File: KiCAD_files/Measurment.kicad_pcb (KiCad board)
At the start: 2 copper layers, 90 x 63 mm, 69 parts, among them J1 Measurment_stage_outline_outp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, J2 Measurment_stage_outline_sign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, J3 Conn_01x02, U1 NMA1505SC, U2 AMC1100, U3 AMC1100, U4 AMC1311, U5 R-78C5.0-1.0, U6 AMS1117-3.3, U7 NMA1505SC

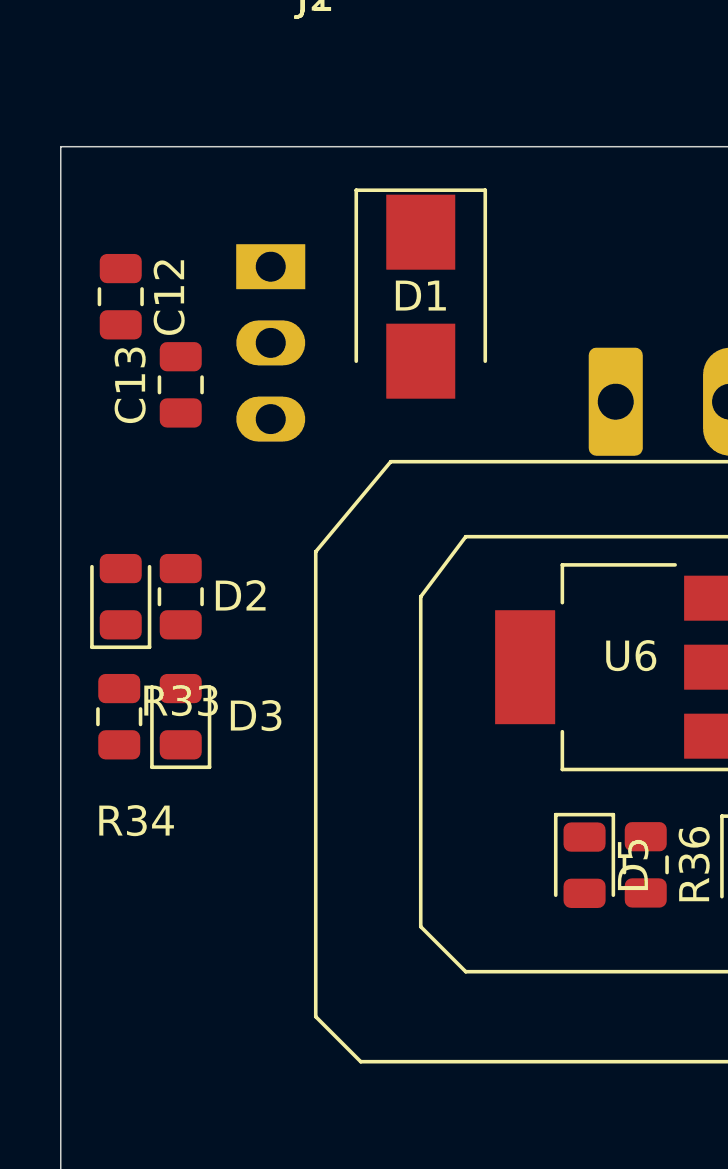
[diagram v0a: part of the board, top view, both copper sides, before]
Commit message: Added alpha version of Nucleo Shield stage - Routed power board
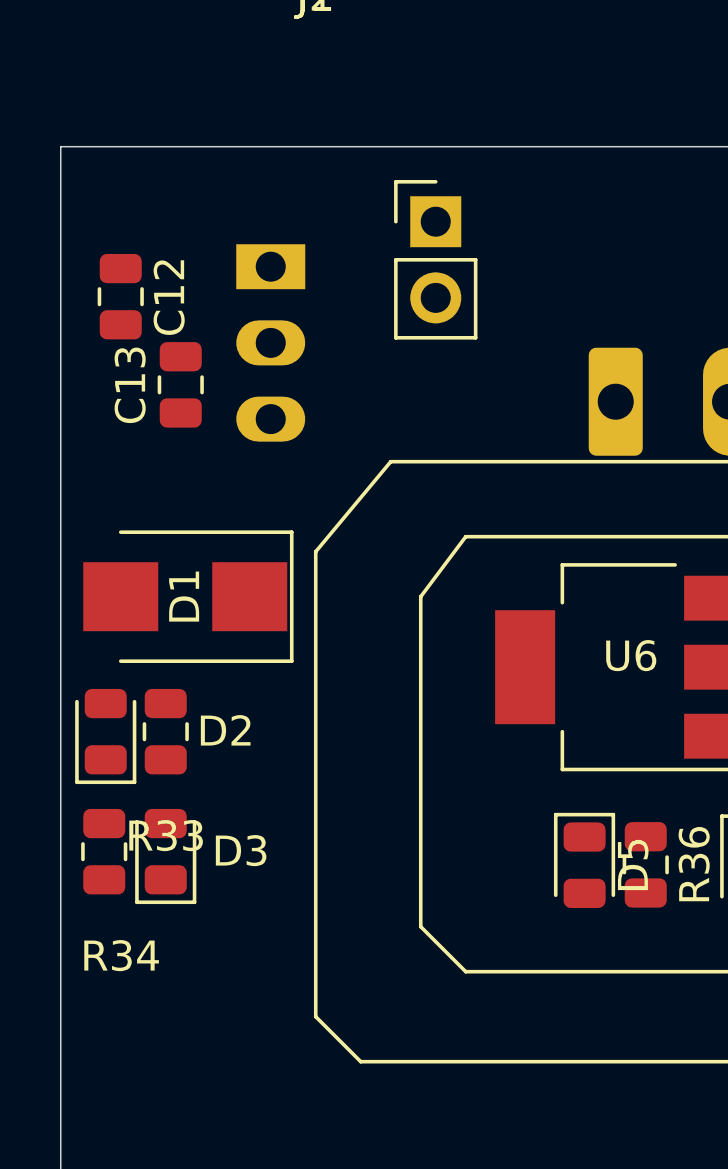
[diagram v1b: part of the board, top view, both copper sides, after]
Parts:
- J1: value Measurment_stage_outline_outputs -> Board outline
- moved D1 12.7 mm to (35.6, 56.5), turned to 180 degrees
- moved D2 4.53 mm to (33.0, 61.0)
- moved D3 4.53 mm to (35.0, 65.0)
- moved R33 4.53 mm to (35.0, 61.0)
- moved R34 4.53 mm to (33.0, 65.0)

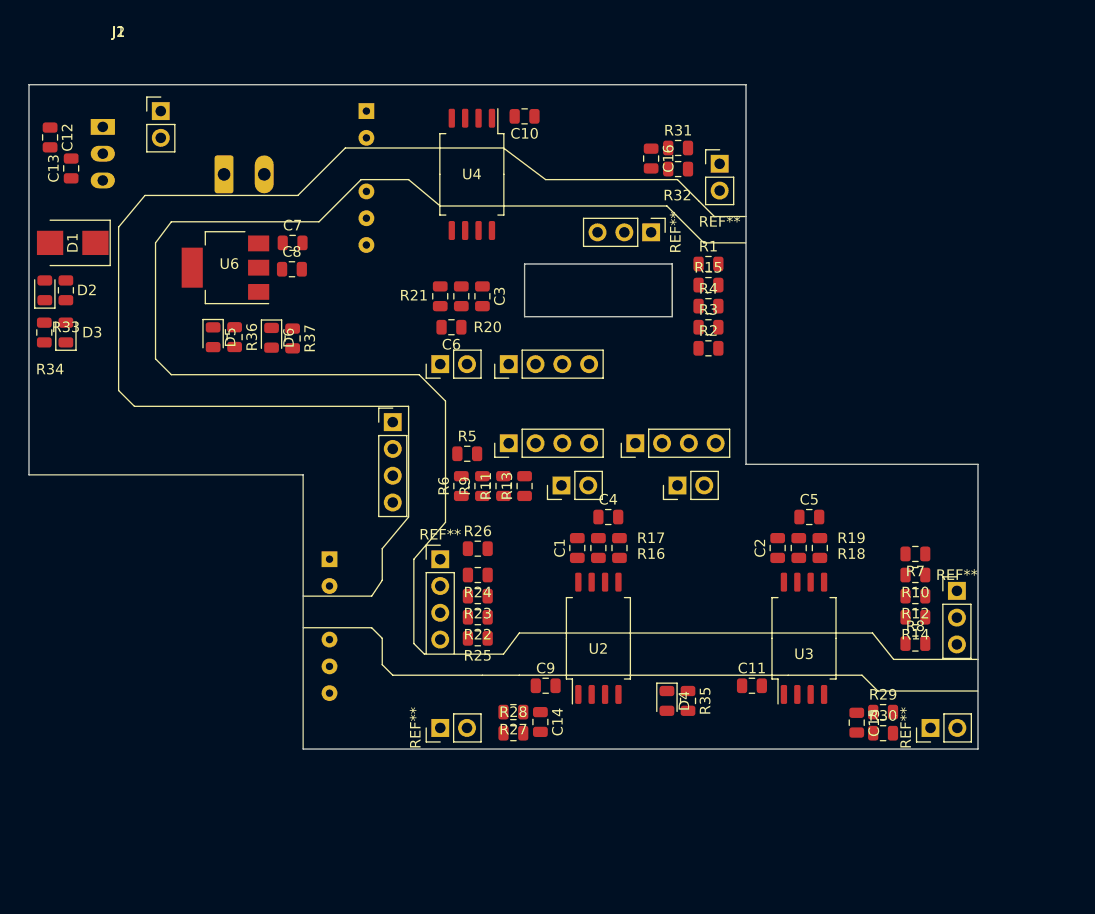
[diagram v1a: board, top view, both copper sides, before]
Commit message: Preliminary routing done - inter layers connectors issues to be solved
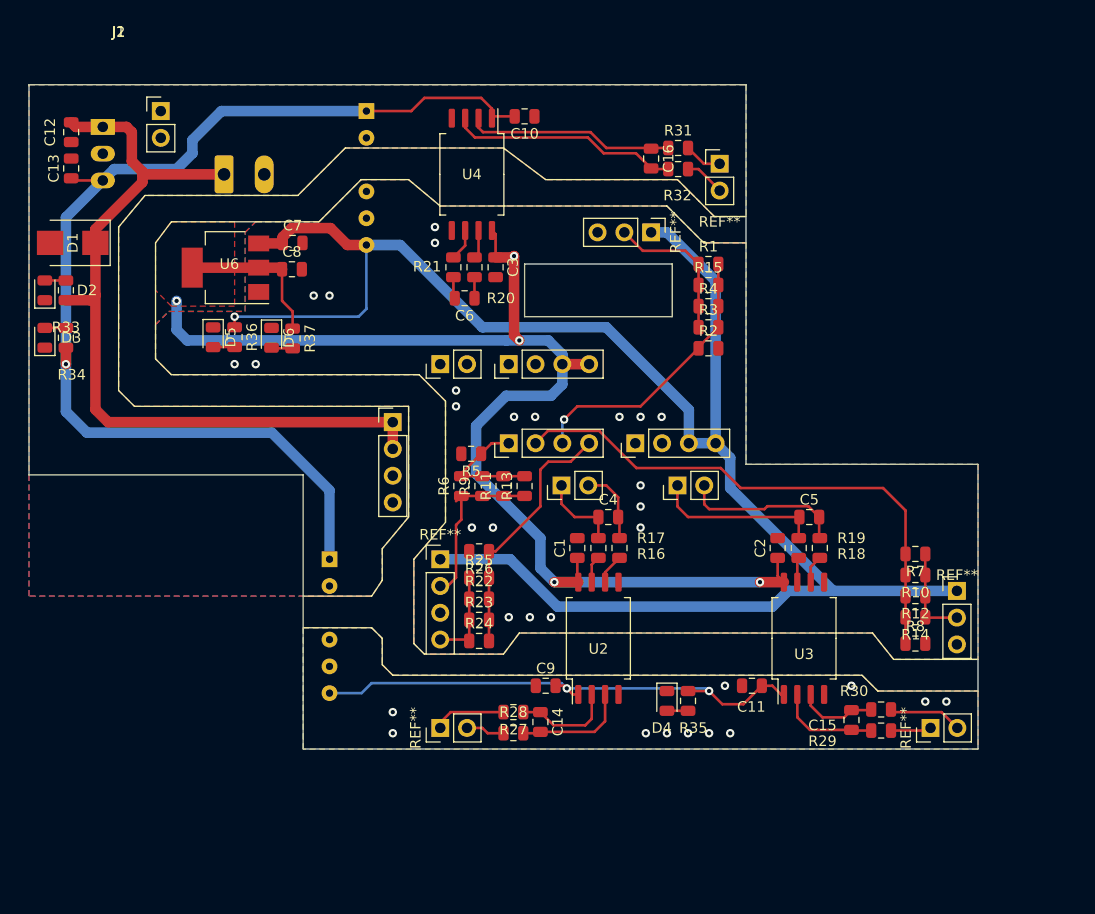
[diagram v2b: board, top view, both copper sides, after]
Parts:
- moved R24 6.25 mm to (74.2, 94.2), turned to 0 degrees
- moved R25 5.75 mm to (74.2, 88.2), turned to 0 degrees
- moved C3 3.02 mm to (75.8, 58.8)
- moved C6 3.02 mm to (72.8, 61.8)
- moved R20 3.02 mm to (73.8, 58.8)
- moved R21 3.02 mm to (71.8, 58.8)
- moved R30 2.26 mm to (112.3, 100.8)
- moved R23 2.25 mm to (74.2, 92.2), turned to 0 degrees
- moved R34 2.11 mm to (35.0, 65.5)
- moved C12 2.06 mm to (35.5, 46.0)
- moved D3 2.06 mm to (33.0, 65.5)
- moved R29 1.76 mm to (112.3, 102.8)
- moved R22 1.75 mm to (74.2, 90.2), turned to 0 degrees
- moved C15 0.56 mm to (109.5, 101.8), turned to 90 degrees
- moved R5 0.38 mm to (73.4, 76.5), turned to 180 degrees
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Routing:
- net +5VD: track 0.00 -> 168.2 mm, vias 0 -> 1
- net +3V3: track 0.00 -> 129.6 mm, vias 0 -> 5
- net +5V: track 0.00 -> 107.1 mm, vias 0 -> 1
- net +15V: track 0.00 -> 76.9 mm
- net /IILow2_ADC: track 0.00 -> 51.3 mm
- net +5P: track 0.00 -> 49.9 mm, vias 0 -> 2
- net /IIHigh_ADC: track 0.00 -> 26.6 mm, vias 0 -> 1
- net /VTh_ADC: track 0.00 -> 24.3 mm
- net GNDREF: track 0.00 -> 21.8 mm
- net Net-(C16-Pad1): track 0.00 -> 19.7 mm
- net /IILow1: track 0.00 -> 16.5 mm
- net /VILow2+_ADC: track 0.00 -> 16.0 mm
- net /VILow2_ADC: track 0.00 -> 15.4 mm
- net /IIHigh: track 0.00 -> 14.3 mm
- net /IILow1_ADC: track 0.00 -> 11.9 mm
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- added copper zone on F.Cu, net +3V3
- added copper zone on B.Cu, net /N
- added copper zone on F.Cu, net /N
- added copper zone on B.Cu, net GNDD
- added copper zone on F.Cu, net GNDD
- added copper zone on B.Cu, net GNDREF
- added copper zone on F.Cu, net GNDREF

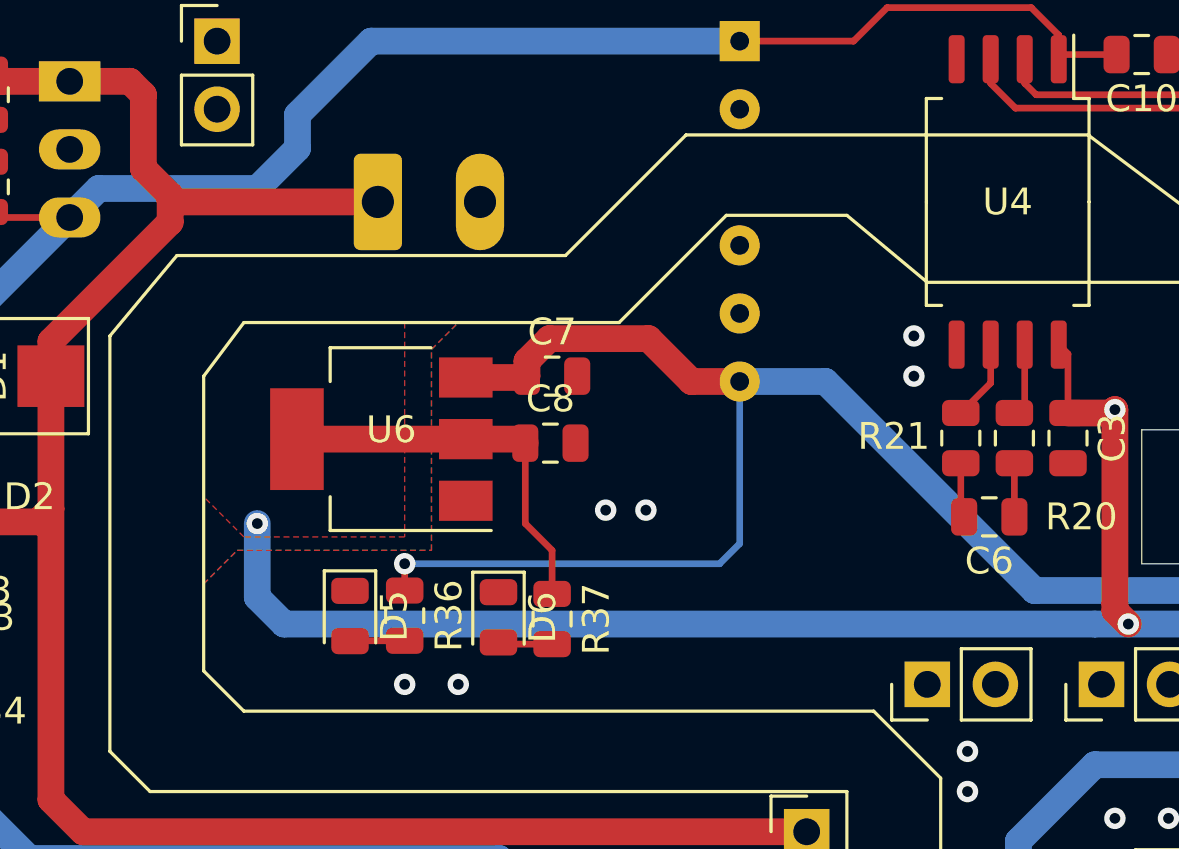
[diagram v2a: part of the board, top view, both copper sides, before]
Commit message: Improved power board traces - Took a power electronic routing guideline into consideration.
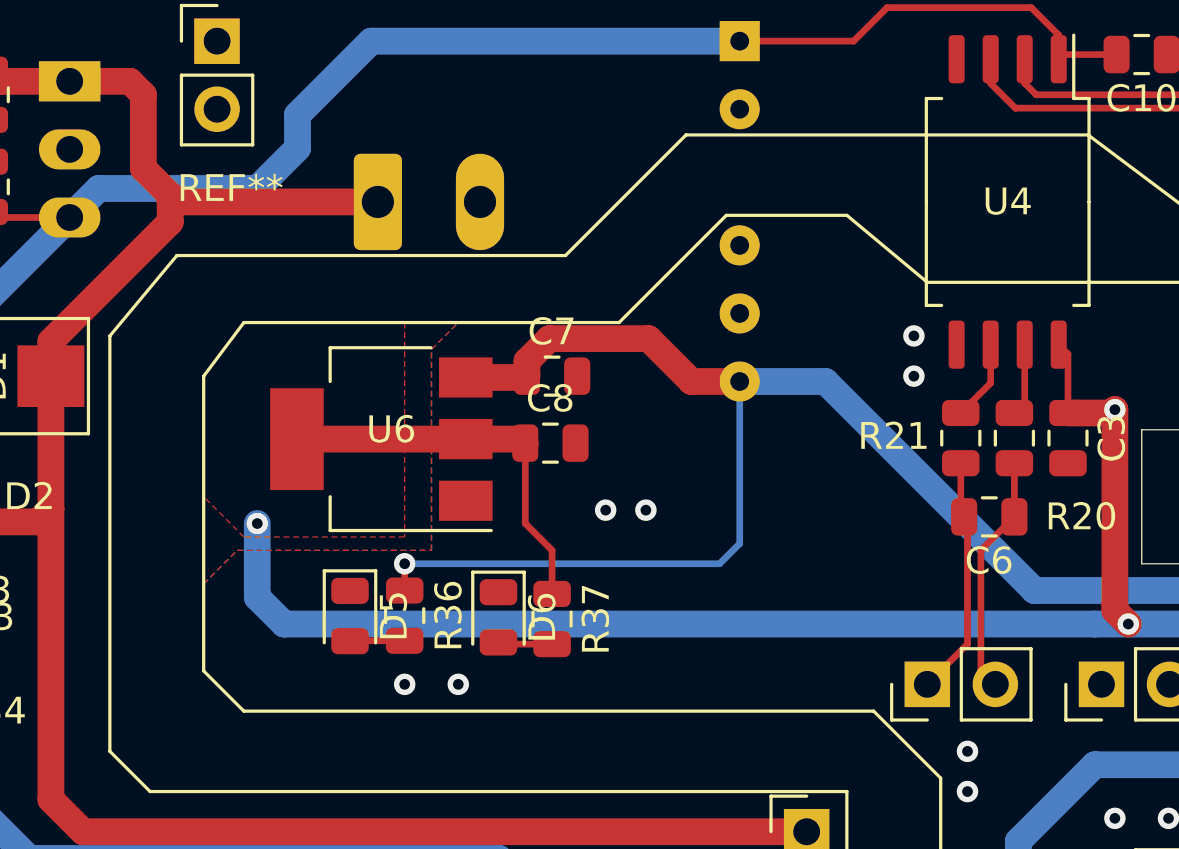
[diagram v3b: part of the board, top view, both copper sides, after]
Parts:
- J1: value Board outline -> Measurment_stage_outline_outputs
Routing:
- net /VIHigh+_ADC: track 2.00 -> 8.99 mm
- net /VIHigh-_ADC: track 2.05 -> 8.97 mm

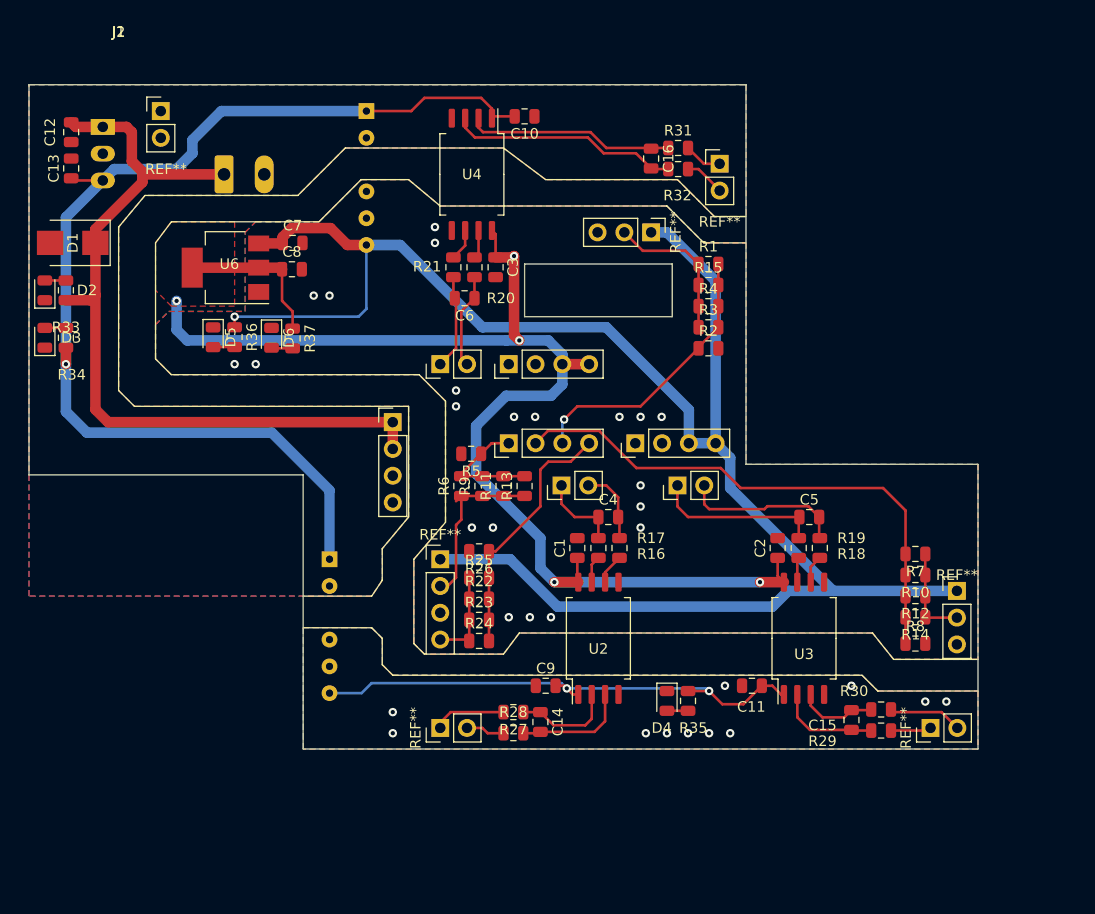
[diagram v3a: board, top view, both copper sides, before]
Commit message: Added optional film caps - Added Heatsink mounting holes Verified mezzanine electrical connexions.
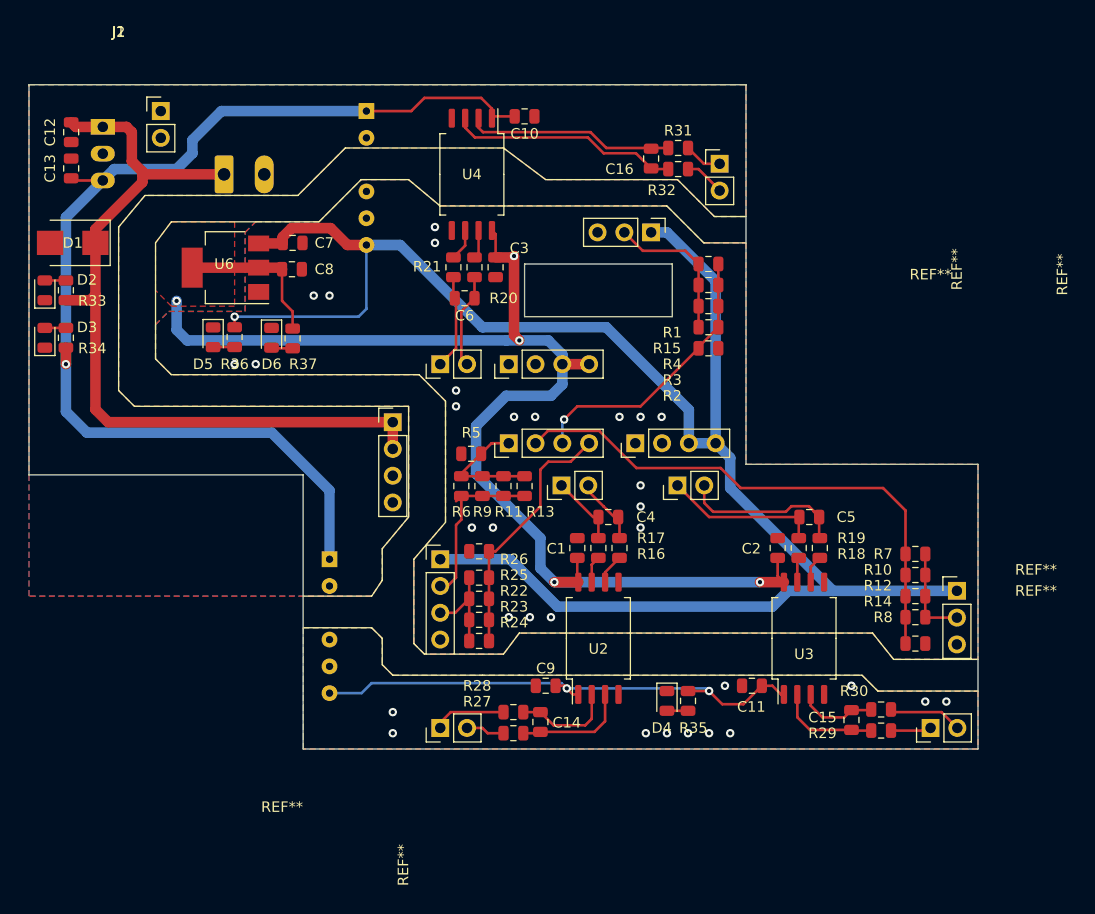
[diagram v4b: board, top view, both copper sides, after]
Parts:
- J1: value Measurment_stage_outline_outputs -> Board outline
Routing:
- net /VILow2+_ADC: track 16.0 -> 14.8 mm
- net /VILow1+_ADC: track 7.77 -> 6.74 mm
- net /VILow1-_ADC: track 7.23 -> 6.45 mm
- net /VTh: track 8.80 -> 9.48 mm
